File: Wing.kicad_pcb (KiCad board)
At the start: 2 copper layers, 73.3 x 42.5 mm, 9 parts, among them J2 6pin_conn

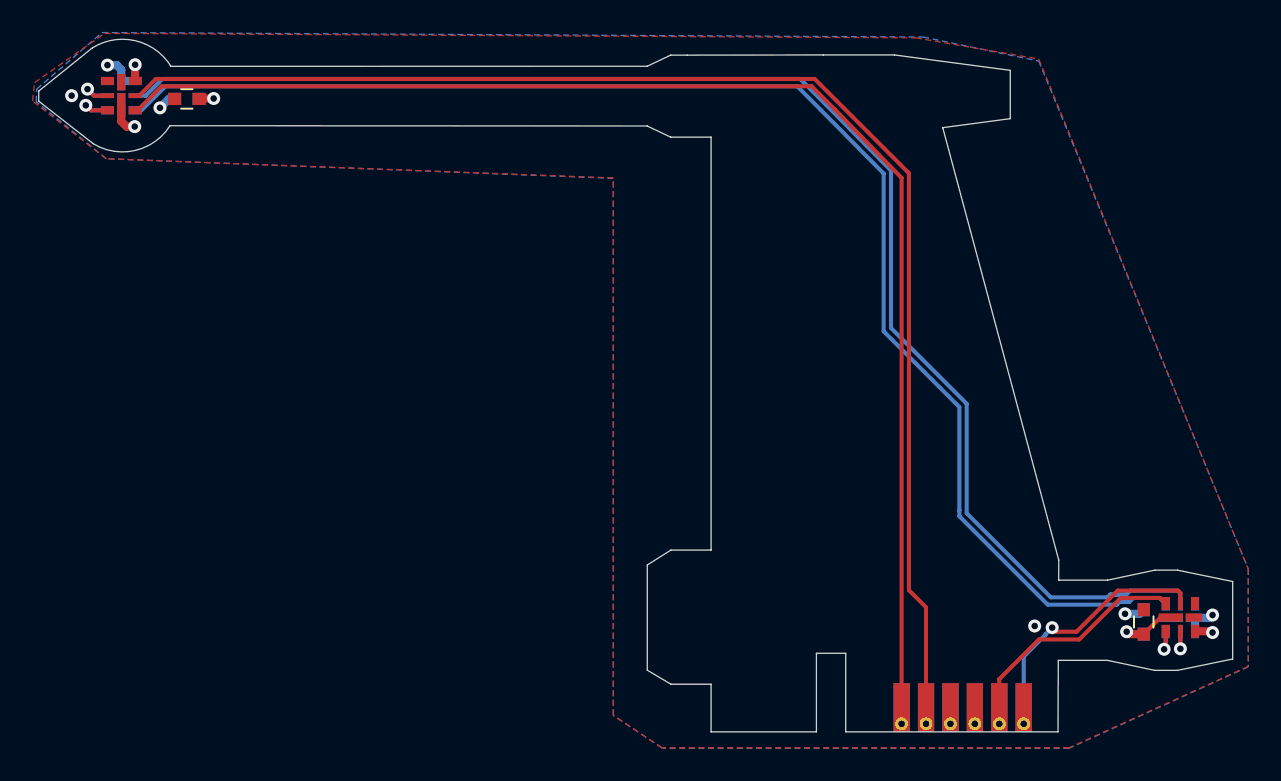
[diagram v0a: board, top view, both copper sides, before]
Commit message: Board Fixes fort bad footprint
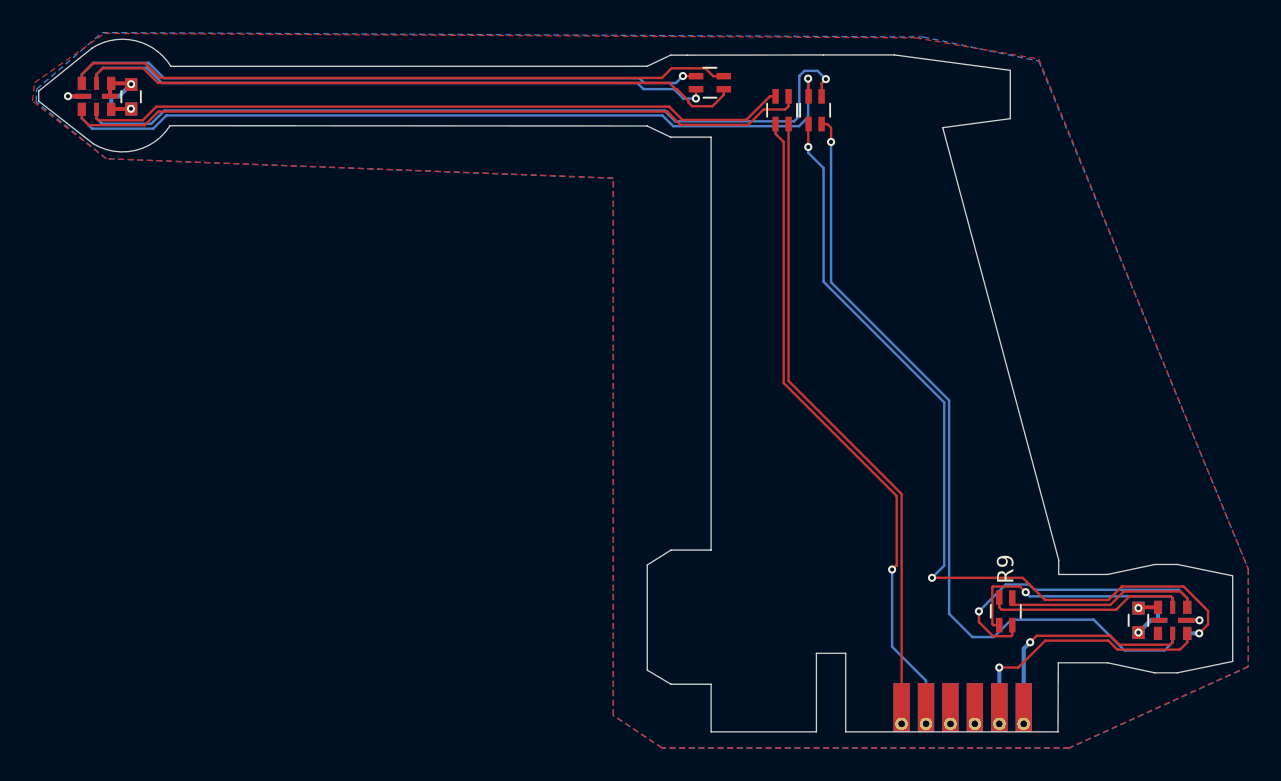
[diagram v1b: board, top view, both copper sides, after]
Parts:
- added R6: 33 ohm, Resistors_SMD:R_Array_Concave_2x0603, F.Cu at (147.9, 61.4)
- added R7: 33 ohm, Resistors_SMD:R_Array_Concave_2x0603, F.Cu at (143.4, 59.7)
- added R8: 33 ohm, Resistors_SMD:R_Array_Concave_2x0603, F.Cu at (149.9, 61.4)
- added R9: 33 ohm, Resistors_SMD:R_Array_Concave_2x0603, F.Cu at (161.6, 92.1)
- D5, D6, D7, D8: footprint MyLib:APA102-2020 -> MyLib:APA102-2020_style_2
- moved C6 3.42 mm to (107.9, 60.5), turned to 270 degrees
- moved C8 3.42 mm to (107.9, 60.5), turned to 270 degrees
- moved D5 1.52 mm to (105.8, 60.5), turned to 270 degrees
- moved D6 1.52 mm to (105.8, 60.5), turned to 90 degrees
- moved D8 0.51 mm to (171.8, 92.7), turned to 90 degrees
- moved D7 0.50 mm to (171.8, 92.7), turned to 270 degrees
- moved C5 0.34 mm to (169.7, 92.7), turned to 90 degrees
- moved C7 0.34 mm to (169.7, 92.7), turned to 90 degrees
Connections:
- D6 pad 4: Net-(D5-Pad3) -> Net-(D6-Pad4)
- D6 pad 5: Net-(D5-Pad2) -> Net-(D6-Pad5)
- D7 pad 4: Net-(D6-Pad3) -> Net-(D7-Pad4)
- D7 pad 5: Net-(D6-Pad2) -> Net-(D7-Pad5)
- D8 pad 4: Net-(D7-Pad3) -> Net-(D8-Pad4)
- D8 pad 5: Net-(D7-Pad2) -> Net-(D8-Pad5)
- J2 pad 1: Net-(D5-Pad4) -> Net-(J2-Pad1)
- J2 pad 2: Net-(D5-Pad5) -> Net-(J2-Pad2)
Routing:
- net Net-(D7-Pad4): track 0.00 -> 52.5 mm, vias 0 -> 3
- net Net-(D7-Pad5): track 0.00 -> 49.8 mm, vias 0 -> 1
- net Net-(J2-Pad1): track 0.00 -> 40.7 mm
- net Net-(D5-Pad5): track 83.6 -> 43.6 mm
- net Net-(J2-Pad2): track 0.00 -> 39.9 mm, vias 0 -> 1
- net Net-(D6-Pad4): track 0.00 -> 39.3 mm, vias 0 -> 1
- net Net-(D6-Pad2): track 89.3 -> 50.2 mm, vias 0 -> 1
- net Net-(D6-Pad5): track 0.00 -> 38.9 mm, vias 0 -> 1
- net Net-(D5-Pad3): track 2.91 -> 41.1 mm, vias 1 -> 0
- net Net-(D5-Pad2): track 2.78 -> 40.9 mm, vias 1 -> 0
- net Net-(D5-Pad4): track 83.6 -> 45.9 mm
- net Net-(D6-Pad3): track 87.0 -> 49.7 mm, vias 0 -> 1
- net Net-(D7-Pad3): track 2.26 -> 18.1 mm
- net Net-(D7-Pad2): track 2.12 -> 14.7 mm
- net Net-(D8-Pad4): track 0.00 -> 12.4 mm
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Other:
- outline, holes or cut-outs redrawn
- net class Min added: clearance 0.15, trace_width 0.15, via_dia 0.8, via_drill 0.4
- rule trace_min: 0.2 -> 0.127
- rule via_min_drill: 0.3 -> 0.2
